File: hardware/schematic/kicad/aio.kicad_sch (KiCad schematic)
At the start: 0 parts

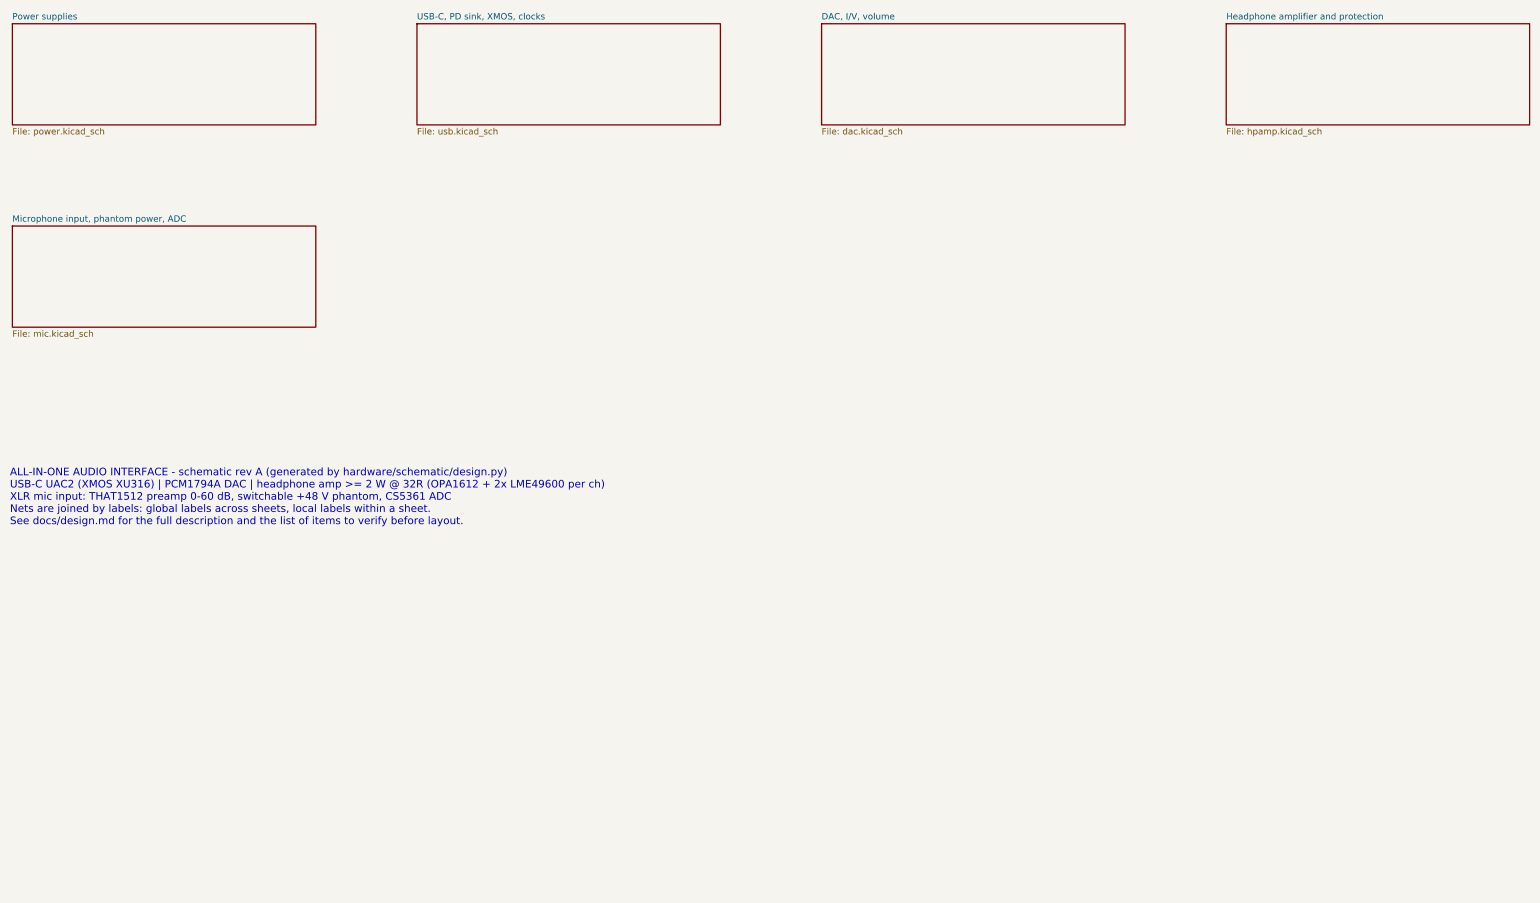
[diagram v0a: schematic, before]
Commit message: Split schematic into 14 A3 sheets, fix board outline, cluster placement
- Schematic: the five large A1/A0 sheets become 14 A3 sheets, one per
  function. Designators are unchanged (sections share one numbering
  sequence); the BOM is identical.
- PCB staging board: the outline was computed from board edges before any
  existed, so it came out far too small. It now encloses all parts. Parts
  are packed into one labelled cluster per sheet instead of one long strip.
- README: Altium steps for the "Missing child-sheet" errors (drop the top
  sheet, use global net scope) and layout guidance: don't autoroute the
  staging board.
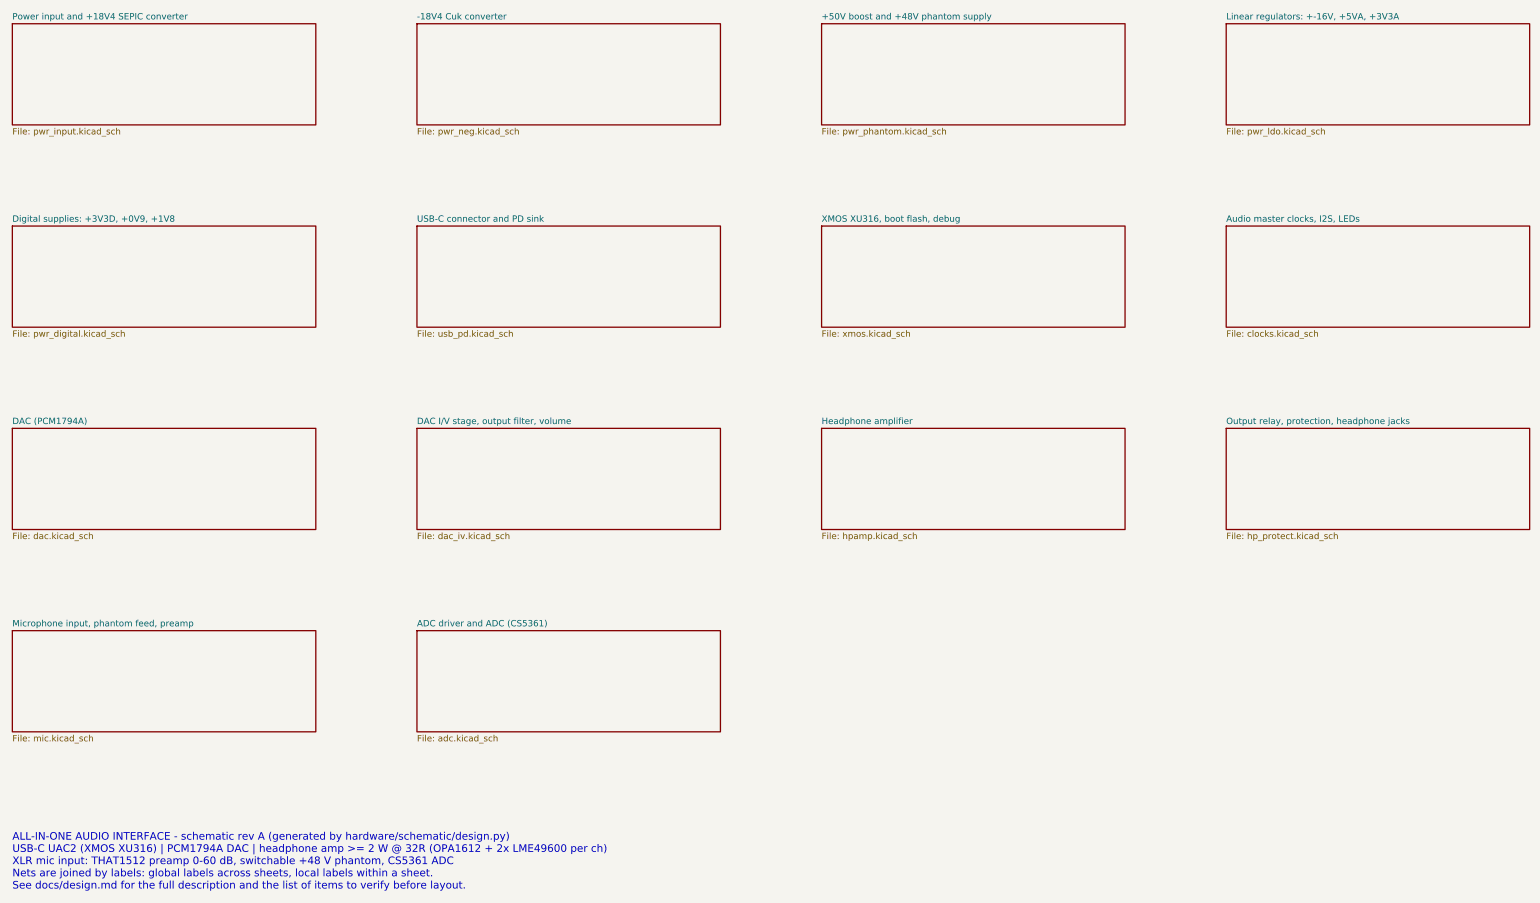
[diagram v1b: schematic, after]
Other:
- sheet DAC, I/V, volume renamed DAC (PCM1794A)
- sheet Headphone amplifier and protection renamed Headphone amplifier
- sheet Microphone input, phantom power, ADC renamed Microphone input, phantom feed, preamp
- removed sheet Power supplies
- removed sheet USB-C, PD sink, XMOS, clocks
- added sheet +50V boost and +48V phantom supply (pwr_phantom.kicad_sch)
- added sheet -18V4 Cuk converter (pwr_neg.kicad_sch)
- added sheet ADC driver and ADC (CS5361) (adc.kicad_sch)
- added sheet Audio master clocks, I2S, LEDs (clocks.kicad_sch)
- added sheet DAC I/V stage, output filter, volume (dac_iv.kicad_sch)
- added sheet Digital supplies: +3V3D, +0V9, +1V8 (pwr_digital.kicad_sch)
- added sheet Linear regulators: +-16V, +5VA, +3V3A (pwr_ldo.kicad_sch)
- added sheet Output relay, protection, headphone jacks (hp_protect.kicad_sch)
- added sheet Power input and +18V4 SEPIC converter (pwr_input.kicad_sch)
- added sheet USB-C connector and PD sink (usb_pd.kicad_sch)
- added sheet XMOS XU316, boot flash, debug (xmos.kicad_sch)
- title: All-in-one audio interface: USB DAC/amp + phantom-powered mic input -> All-in-one audio interface
